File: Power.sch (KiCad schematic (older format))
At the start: 38 parts, among them IC1 INA181, IC2 INA181, IC3 INA181, U2 IRS2186, U3 IRS2186, U4 IRS2186

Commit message: - corrected current filter resistors - adapted USB footprint - added 0.1% note to dc bus voltage divider
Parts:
- R26, R27, R32: value 470R -> 100R
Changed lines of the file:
@@
 $Descr A4 11693 8268
 encoding utf-8
-Sheet 7 8
+Sheet 5 8
 Title "HSWR MOSFET Driver"
 Date "2017-02-05"
@@
 Wire Wire Line
 	2750 2150 2750 2200
-Connection ~ 2750 2200
 $Comp
 L HSWR-V2-rescue:INA181-Auktoralib IC1
@@
 P 5750 1950
 F 0 "R26" V 5850 1950 50  0000 C CNN
-F 1 "470R" V 5750 1950 50  0000 C CNN
+F 1 "100R" V 5750 1950 50  0000 C CNN
 F 2 "Resistor_SMD:R_0805_2012Metric" V 5680 1950 50  0001 C CNN
 F 3 "~" H 5750 1950 50  0001 C CNN
@@
 Wire Wire Line
 	2450 1700 2450 1350
-Connection ~ 2450 1700
 Connection ~ 2450 1350
 Wire Notes Line
@@
 Wire Wire Line
 	2750 3850 2750 3900
-Connection ~ 2750 3900
 $Comp
 L HSWR-V2-rescue:INA181-Auktoralib IC2
@@
 P 5750 3650
 F 0 "R27" V 5850 3650 50  0000 C CNN
-F 1 "470R" V 5750 3650 50  0000 C CNN
+F 1 "100R" V 5750 3650 50  0000 C CNN
 F 2 "Resistor_SMD:R_0805_2012Metric" V 5680 3650 50  0001 C CNN
 F 3 "~" H 5750 3650 50  0001 C CNN
@@
 Wire Wire Line
 	2450 3400 2450 3050
-Connection ~ 2450 3400
 Connection ~ 2450 3050
 $Comp
@@
 Wire Wire Line
 	2750 5600 2750 5650
-Connection ~ 2750 5650
 Wire Wire Line
 	2300 4800 2450 4800
 Wire Wire Line
 	2450 5150 2450 4800
-Connection ~ 2450 5150
 Connection ~ 2450 4800
 $Comp
@@
 P 5750 5350
 F 0 "R32" V 5850 5350 50  0000 C CNN
-F 1 "470R" V 5750 5350 50  0000 C CNN
+F 1 "100R" V 5750 5350 50  0000 C CNN
 F 2 "Resistor_SMD:R_0805_2012Metric" V 5680 5350 50  0001 C CNN
 F 3 "~" H 5750 5350 50  0001 C CNN

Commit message: first commit of Amalga_100.
R2D needs to be finished.
Logicpart needs to be routed.
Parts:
- removed C20, C21, C22, C23, C24, C25, C26, C27, C28: 1u, Capacitor_SMD:C_0805_2012Metric, symbol Device:C
- removed C29, C30, C31: 4n7, Capacitor_SMD:C_0805_2012Metric, symbol Device:C
- removed C32, C37, C38: 100n, Capacitor_SMD:C_0805_2012Metric, symbol Device:C
- removed D4, D5: RFN2L4S, Diode_SMD:D_SOD-123, symbol Device:D_Small
- removed IC1, IC2, IC3: INA181, Package_TO_SOT_SMD:SOT-23-6, symbol HSWR-V2-rescue:INA181-Auktoralib
- removed R21, R24, R25: EWSL3920FL500S9, Resistor_SMD:R_4020_10251Metric, symbol Device:R_Small
- removed R26, R27, R32: 100R, Resistor_SMD:R_0805_2012Metric, symbol Device:R
- removed R33, R34: 1k 0.1%, Resistor_SMD:R_0805_2012Metric, symbol Device:R
- removed R35, R37, R39: 300k 0.1%, Resistor_SMD:R_0805_2012Metric, symbol Device:R
- removed R36, R38, R40: 4k7 0.1%, Resistor_SMD:R_0805_2012Metric, symbol Device:R
- removed U2, U3, U4: IRS2186, Package_SO:SO-8_3.9x4.9mm_P1.27mm, symbol HSWR-V2-rescue:IRS2186-Driver_FET
- added C28, C29, C30, C31, C32, C33: 1u, Capacitor_SMD:C_0805_2012Metric, symbol Amalga_100-rescue:C_Small-Device
- added C39, C41, C62: 10n, Capacitor_SMD:C_0805_2012Metric, symbol Amalga_100-rescue:C-Device
- added C43, C44, C64: 1u, Capacitor_SMD:C_0805_2012Metric, symbol Amalga_100-rescue:C-Device
- added D18, D19: RFN2L4S, Diode_SMD:D_SMA, symbol Amalga_100-rescue:D_Small-Device
- added IC3, IC4, IC5: INA240A1, Package_SO:TSSOP-8_4.4x3mm_P0.65mm, symbol Amalga_100-rescue:INA240-HSWR-V2-rescue
- added R45, R47, R48: CSS2H-3920R-L500, alexmod:CSS3920, symbol Amalga_100-rescue:R-Device
- added R53, R55, R57: 220k, Resistor_SMD:R_0805_2012Metric, symbol Amalga_100-rescue:R-RESCUE-BLDC_4-HSWR-V2-rescue
- added R54, R56, R58: 3k3, Resistor_SMD:R_0805_2012Metric, symbol Amalga_100-rescue:R-RESCUE-BLDC_4-HSWR-V2-rescue
- added U7, U8, U9: IRS2186, Package_SO:SOIC-8_3.9x4.9mm_P1.27mm, symbol Amalga_100-rescue:IRS2186-Driver_FET
- D6: footprint Diode_SMD:D_SOD-123 -> Diode_SMD:D_SMA; symbol Device:D_Small -> Amalga_100-rescue:D_Small-Device
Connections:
- net labels added: +15V, BR_SO1, BR_SO2, BR_SO3, H1_LOW, H1_VS, H1_out, H1_pwm, H2_LOW, H2_VS, H2_out, H2_pwm, H3_LOW, H3_VS, H3_out, H3_pwm, L1_out, L1_pwm, L2_out, L2_pwm, L3_out, L3_pwm, SENS1, SENS2, SENS3
- net labels removed: +12V, U2_REF, U_GH, U_GL, U_I, U_PWM_H, U_PWM_L, U_U, U_VP, U_VS, V_GH, V_GL, V_I, V_PWM_H, V_PWM_L, V_U, V_VP, V_VS, W_GH, W_GL, W_I, W_PWM_H, W_PWM_L, W_U, W_VP, W_VS
- wire segments 70 -> 99
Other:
- note added: "Bootstrap Kondensator größer? 2u?"
- note added: "Diode bis 1200 V nötig (?)\n"

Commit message: made Bom (BomAmalga_Kosten.xlsx) Backup
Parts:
- C31, C32, C33: value 1u -> 1u 600V
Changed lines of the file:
@@
 P 7200 1700
 F 0 "C31" H 7250 1850 50  0000 L CNN
-F 1 "1u" H 7100 1500 50  0000 L CNN
+F 1 "1u 600V" H 7100 1500 50  0000 L CNN
 F 2 "Capacitor_SMD:C_0805_2012Metric" H 7200 1700 50  0001 C CNN
 F 3 "" H 7200 1700 50  0000 C CNN
@@
 P 7250 3500
 F 0 "C32" H 7300 3650 50  0000 L CNN
-F 1 "1u" H 7150 3300 50  0000 L CNN
+F 1 "1u 600V" H 7150 3300 50  0000 L CNN
 F 2 "Capacitor_SMD:C_0805_2012Metric" H 7250 3500 50  0001 C CNN
 F 3 "" H 7250 3500 50  0000 C CNN
@@
 P 7300 5400
 F 0 "C33" H 7350 5550 50  0000 L CNN
-F 1 "1u" H 7400 5450 50  0000 L CNN
+F 1 "1u 600V" H 7400 5450 50  0000 L CNN
 F 2 "Capacitor_SMD:C_0805_2012Metric" H 7300 5400 50  0001 C CNN
 F 3 "" H 7300 5400 50  0000 C CNN

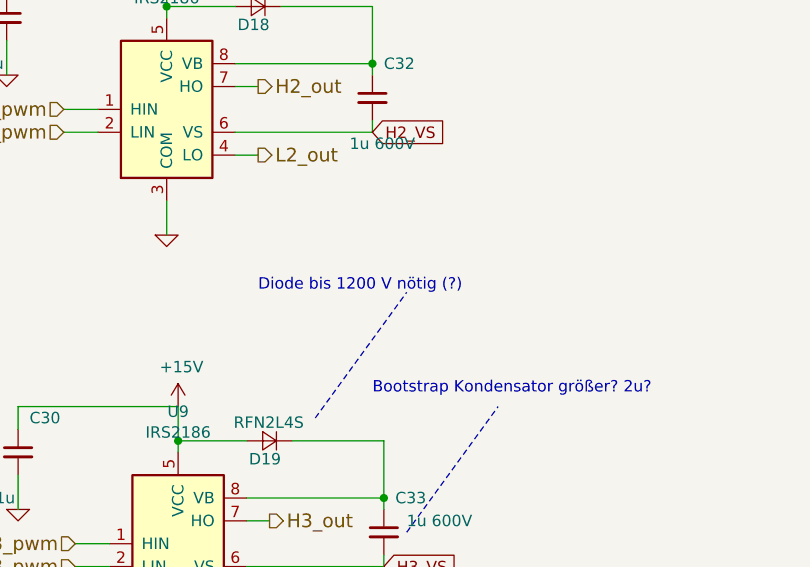
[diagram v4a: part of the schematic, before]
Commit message: -tidied up resolver circuit (need voltage detection on reset pin. >10µs, low active)
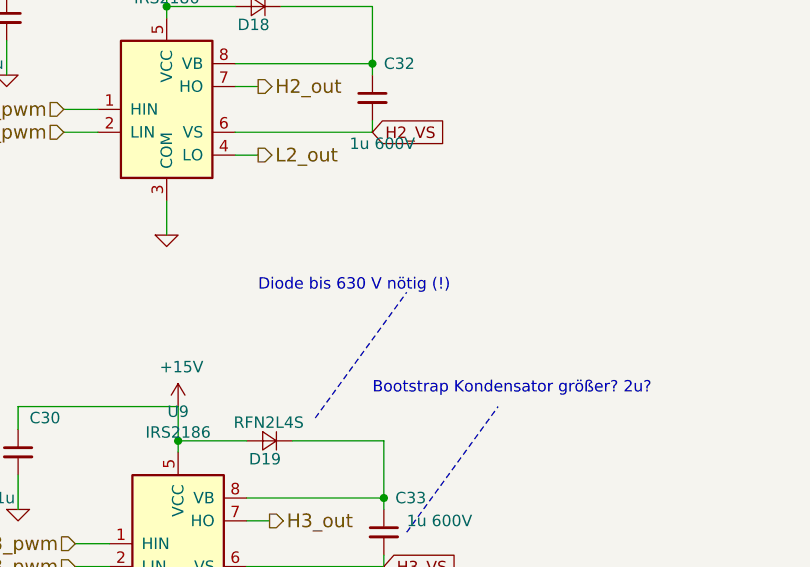
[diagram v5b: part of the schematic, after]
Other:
- note added: "Diode bis 630 V nötig (!)\n"
- note removed: "Diode bis 1200 V nötig (?)\n"
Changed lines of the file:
@@
 EESchema Schematic File Version 4
 LIBS:Amalga_100-cache
-EELAYER 26 0
+EELAYER 29 0
 EELAYER END
 $Descr A4 11693 8268
@@
 	7000 4900 7400 4350
 Text Notes 6750 4350 0    50   ~ 0
-Diode bis 1200 V nötig (?)\n
+Diode bis 630 V nötig (!)\n
 Wire Wire Line
 	1650 6150 2400 6150

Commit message: added dc-bias for adc sin/cos resolver
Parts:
- R48: footprint alexmod:CSS3920 -> Resistor_SMD:R_4020_10251Metric_Pad1.65x5.30mm_HandSolder
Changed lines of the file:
@@
 F 0 "R48" V 1780 1850 50  0000 C CNN
 F 1 "CSS2H-3920R-L500" V 1900 2050 50  0000 C CNN
-F 2 "alexmod:CSS3920" V 1630 1850 50  0001 C CNN
+F 2 "Resistor_SMD:R_4020_10251Metric_Pad1.65x5.30mm_HandSolder" V 1630 1850 50  0001 C CNN
 F 3 "" H 1700 1850 50  0000 C CNN
 	1    1700 1850

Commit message: -changed ad2s1200 to ad2s1205  (pin compatibel) -changed excitation-buffer circuit. (AD8397 in use now) -fixed thermal-connections of planes
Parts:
- R45, R47: footprint alexmod:CSS3920 -> eigene_mod:CSS3920
- R48: footprint Resistor_SMD:R_4020_10251Metric_Pad1.65x5.30mm_HandSolder -> eigene_mod:CSS3920
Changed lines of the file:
@@
 EESchema Schematic File Version 4
 LIBS:Amalga_100-cache
-EELAYER 26 0
+EELAYER 29 0
 EELAYER END
 $Descr A4 11693 8268
@@
 F 0 "R48" V 1780 1850 50  0000 C CNN
 F 1 "CSS2H-3920R-L500" V 1900 2050 50  0000 C CNN
-F 2 "Resistor_SMD:R_4020_10251Metric_Pad1.65x5.30mm_HandSolder" V 1630 1850 50  0001 C CNN
+F 2 "eigene_mod:CSS3920" V 1630 1850 50  0001 C CNN
 F 3 "" H 1700 1850 50  0000 C CNN
 	1    1700 1850
@@
 F 0 "R47" V 1730 6300 50  0000 C CNN
 F 1 "CSS2H-3920R-L500" V 1900 6500 50  0000 C CNN
-F 2 "alexmod:CSS3920" V 1580 6300 50  0001 C CNN
+F 2 "eigene_mod:CSS3920" V 1580 6300 50  0001 C CNN
 F 3 "" H 1650 6300 50  0000 C CNN
 	1    1650 6300
@@
 F 0 "R45" V 1780 4150 50  0000 C CNN
 F 1 "CSS2H-3920R-L500" V 1900 4350 50  0000 C CNN
-F 2 "alexmod:CSS3920" V 1630 4150 50  0001 C CNN
+F 2 "eigene_mod:CSS3920" V 1630 4150 50  0001 C CNN
 F 3 "" H 1700 4150 50  0000 C CNN
 	1    1700 4150
